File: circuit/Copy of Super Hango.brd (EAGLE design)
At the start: 259.3 x 146.3 mm, 12 parts, among them M1 MOTOR_DG01D, M2 MOTOR_DG01D, U1 ARDUINO-UNO-R3-SHIELD, U2 L293E

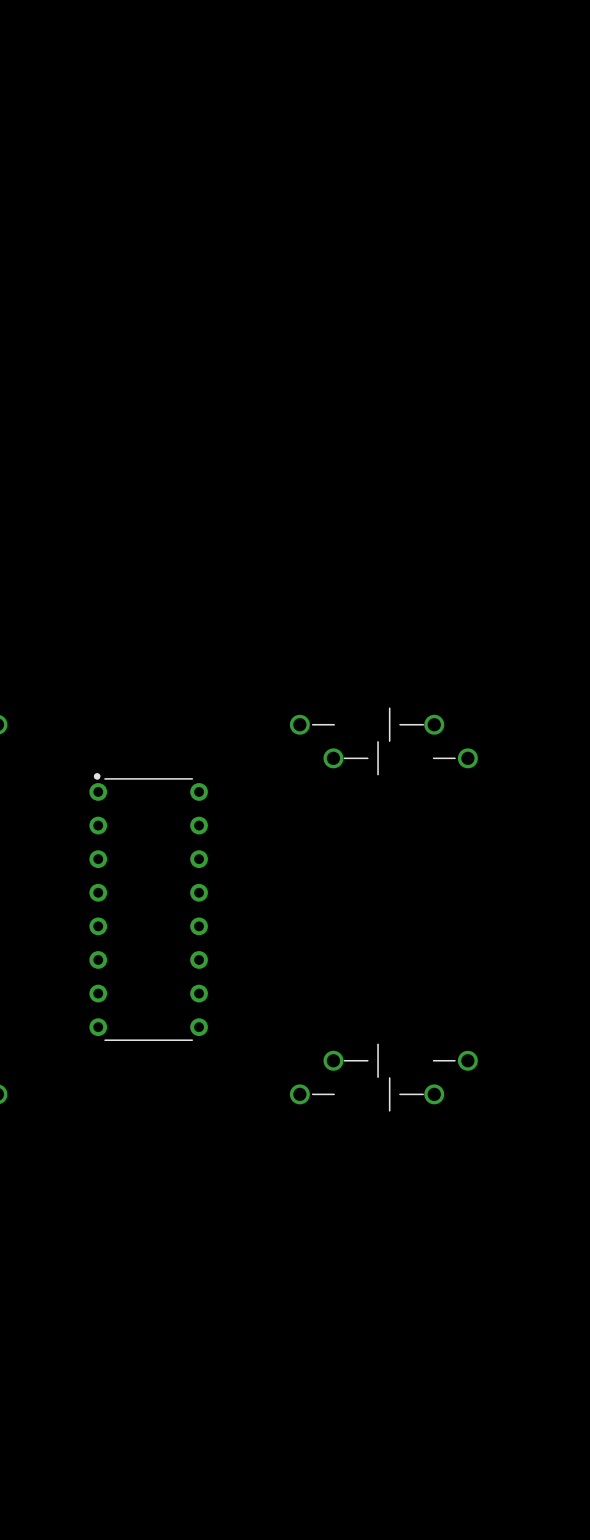
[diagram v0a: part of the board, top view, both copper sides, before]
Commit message: chore: (update) circuit with inverter and sensors
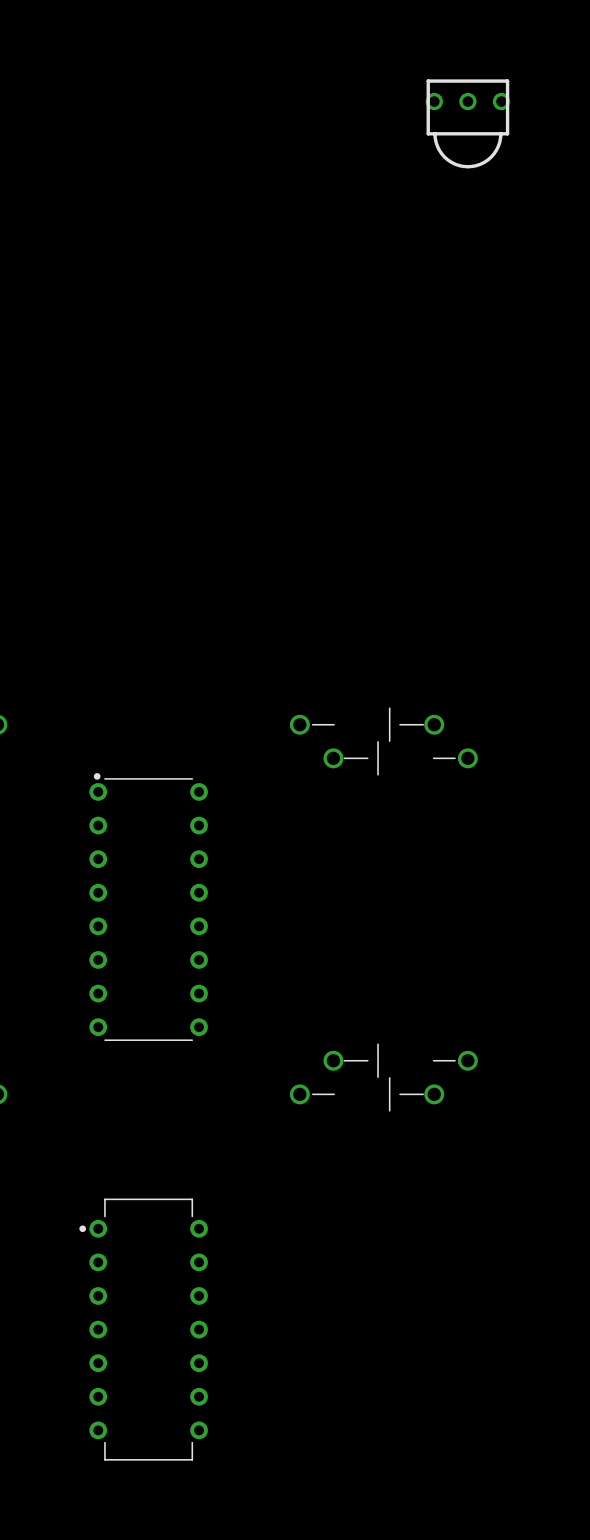
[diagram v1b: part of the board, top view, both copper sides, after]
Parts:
- added U3: 74HC04_PDIP, Tinkercad:DIP762W53P254L1969H508Q14B
- added U5: IR-RECEIVERTSOP48, Tinkercad:TSOP48
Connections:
- removed net U1_D2: U1.D2, U2.2
- removed net U1_D8: U1.D8, U2.10
- new net U1_A0: U1.A0, U5.2
- new net U2_2A: U2.7, U3.2
- new net U2_3A: U2.10, U3.12
- net U1_5V: now also U3.14, U5.3
- net U1_D3: now also U3.13
- net U1_D7: now also U2.2, U3.1; no longer U2.7
- net U1_GND: now also U3.7, U5.1
